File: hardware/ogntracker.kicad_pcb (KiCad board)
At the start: 2 copper layers, 82.7 x 56.6 mm, 54 parts, among them J1 ANT, J2 Micro USB, J3 IGC, U1 LM2936-3.3, Y1 12M

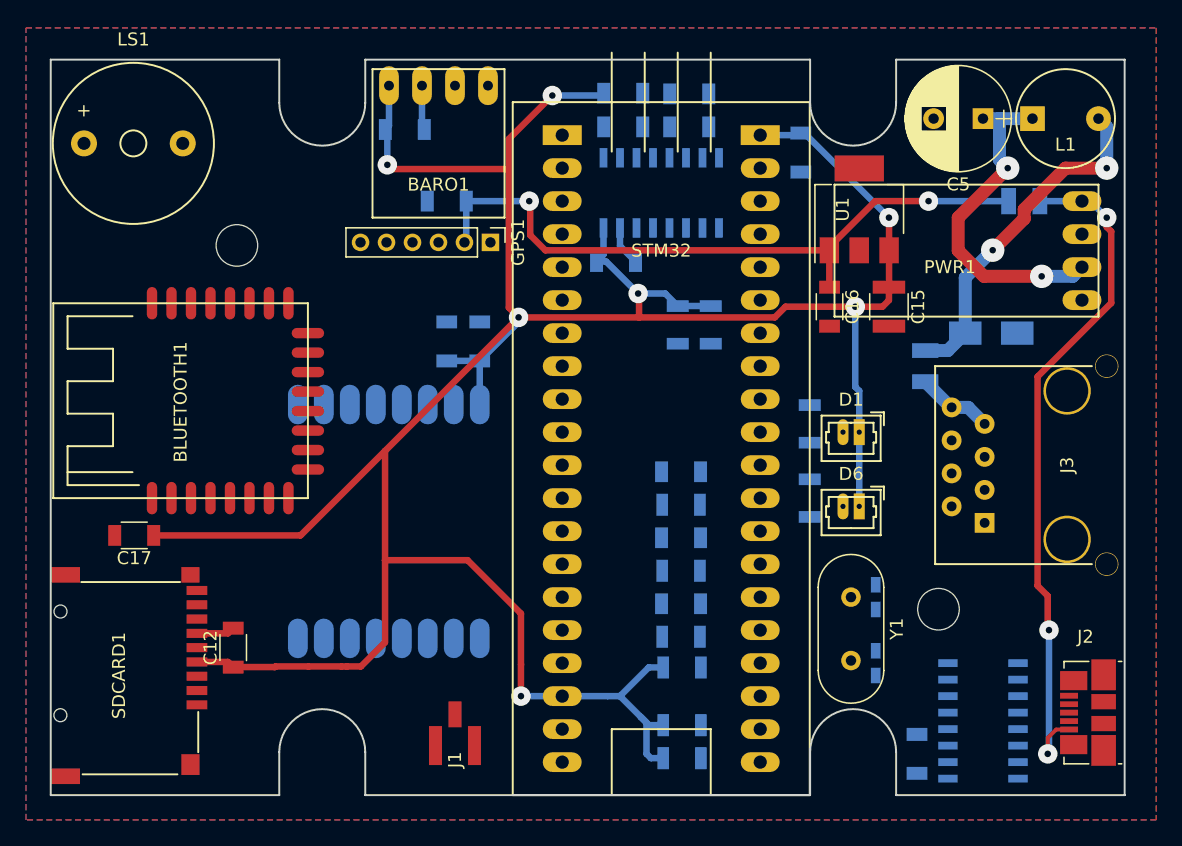
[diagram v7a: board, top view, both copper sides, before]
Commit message: Unverified attempt on standalone STM32 chip
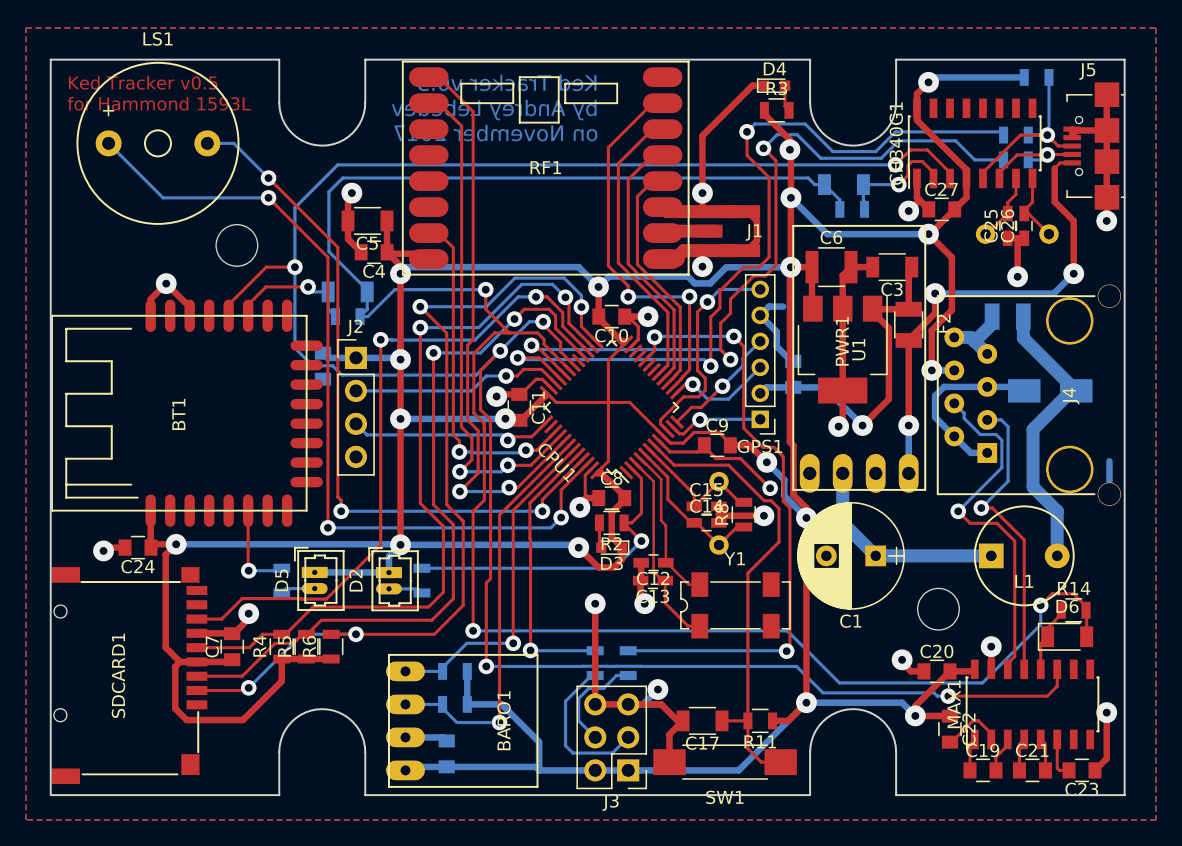
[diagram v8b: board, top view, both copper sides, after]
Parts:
- removed BLUETOOTH1: JDY-08, OGN Tracker:JDY-08
- removed MAX232: MAX3232, Housings_SOIC:SOIC-16_3.9x9.9mm_Pitch1.27mm
- removed RFM69HW1: RFM69HW, OGN Tracker:RFM69HW
- removed STM32: STM32DEVBOARD, OGN Tracker:STM32DEVBOARD_HandSoldering
- added BT1: JDY-08, OGN Tracker:JDY-08, F.Cu at (119.7, 78.1)
- added C19: 100nF, Capacitors_SMD:C_0805, F.Cu at (171.8, 98.1)
- added C20: 100nF, Capacitors_SMD:C_0805, F.Cu at (168.2, 90.5)
- added C21: 100nF, Capacitors_SMD:C_0805, F.Cu at (175.6, 98.1)
- added C22: 100nF, Capacitors_SMD:C_0805, F.Cu at (169.2, 94.9)
- added C23: 100nF, Capacitors_SMD:C_0805, F.Cu at (179.4, 98.1)
- added C24: 100nF, Capacitors_SMD:C_0805, F.Cu at (106.7, 81.0)
- added C25: 22pF, Capacitors_SMD:C_0603_HandSoldering, F.Cu at (173.7, 56.2)
- added C26: 22pF, Capacitors_SMD:C_0603_HandSoldering, F.Cu at (174.9, 56.2)
- added C27: 100nF, Capacitors_SMD:C_0805, F.Cu at (168.6, 54.9)
- added CPU1: STM32F103, Housings_QFP:LQFP-48_7x7mm_Pitch0.5mm, F.Cu at (143.2, 70.2)
- added D7: 1N4148, Diodes_SMD:D_1206, B.Cu at (122.9, 61.3)
- added D8: 1N4148, Diodes_SMD:D_1206, B.Cu at (161.1, 53.0)
- added J4: IGC, OGN Tracker:RJ45_SOCKET_SHLD, F.Cu at (178.4, 69.2)
- added J5: Micro USB, OGN Tracker:USB_Micro, F.Cu at (179.9, 50.0)
- added MAX1: MAX3232, Housings_SOIC:SOIC-16_3.9x9.9mm_Pitch1.27mm, F.Cu at (175.6, 93.0)
- added R11: 10K, Resistors_SMD:R_0805, F.Cu at (154.6, 94.3)
- added R12: 10K, Resistors_SMD:R_0805, B.Cu at (141.9, 89.8)
- added R13: 10K, Resistors_SMD:R_0805, B.Cu at (144.4, 89.8)
- added R14: 10K, Resistors_SMD:R_0805, F.Cu at (178.7, 85.8)
- added R15: 10K, Resistors_SMD:R_0805, B.Cu at (122.9, 63.2)
- added R16: 10K, Resistors_SMD:R_0805, B.Cu at (161.7, 54.9)
- added R17: 20, Resistors_SMD:R_0805, B.Cu at (174.3, 49.2)
- added R18: 20, Resistors_SMD:R_0805, B.Cu at (174.3, 51.1)
- added R19: 1.5K, Resistors_SMD:R_0805, B.Cu at (175.9, 44.8)
- added RF1: RFM69HW, OGN Tracker:RFM69HW, F.Cu at (138.1, 51.7)
- added SW1: RESET, Buttons_Switches_SMD:SW_SPST_REED_CT05-XXXX-G1, F.Cu at (151.9, 97.5)
- added Y2: 8MHz, Crystals:Crystal_HC49-4H_Vertical, B.Cu at (151.4, 80.8)
- added Y3: 12M, Crystals:Crystal_HC49-4H_Vertical, B.Cu at (176.8, 56.8)
- C1: value 100nF -> 330uF; footprint Capacitors_SMD:C_1206 -> Capacitors_ThroughHole:CP_Radial_D8.0mm_P3.80mm; moved to F.Cu
- C10, C11, C7, C8, C9: footprint Capacitors_SMD:C_1206 -> Capacitors_SMD:C_0805; moved to F.Cu
- C12: value 100nF -> 22pF; footprint Capacitors_SMD:C_1206 -> Capacitors_SMD:C_0603_HandSoldering
- C13, C14, CH340G1, F2: moved to F.Cu
- C15: value 47uF -> 22pF; footprint Capacitors_SMD:C_1210 -> Capacitors_SMD:C_0603_HandSoldering
- C16: value 1uF -> 100nF; footprint Capacitors_SMD:C_1206 -> Capacitors_SMD:C_0805; moved to B.Cu
- C17: value 100nF -> 1uF
- C18: footprint Capacitors_SMD:C_1206 -> Capacitors_SMD:C_0805
- C2: value 1uF -> 100nF; footprint Capacitors_SMD:C_1206 -> Capacitors_SMD:C_0805
- C3: value 100nF -> 1uF; moved to F.Cu
- C4: value 1uF -> 100nF; footprint Capacitors_SMD:C_1206 -> Capacitors_SMD:C_0805; moved to F.Cu
- C5: value 330uF -> 1uF; footprint Capacitors_ThroughHole:CP_Radial_D8.0mm_P3.80mm -> Capacitors_SMD:C_1206
- C6: value 100nF -> 47uF; footprint Capacitors_SMD:C_1206 -> Capacitors_SMD:C_1210; moved to F.Cu
- D1: value LED_STAT -> 1N4001; footprint OGN Tracker:Molex_PicoBlade_02x1.25mm_HandSoldering -> Diodes_SMD:D_SMA_Standard; moved to B.Cu
- D2: value 1N4001 -> STATUS_PANEL; footprint Diodes_SMD:D_SMA_Standard -> OGN Tracker:Molex_PicoBlade_02x1.25mm_HandSoldering; moved to F.Cu
- D3: value 1N4148 -> STATUS_SMD; footprint Diodes_SMD:D_1206 -> LEDs:LED_0603; moved to F.Cu
- D4: value 1N4148 -> PWR; footprint Diodes_SMD:D_1206 -> LEDs:LED_0603; moved to F.Cu
- D5: value 1N4148 -> LED_BT; footprint Diodes_SMD:D_1206 -> OGN Tracker:Molex_PicoBlade_02x1.25mm_HandSoldering; moved to F.Cu
- D6: value LED_BT -> 1N4148; footprint OGN Tracker:Molex_PicoBlade_02x1.25mm_HandSoldering -> Diodes_SMD:D_1206
- J2: value Micro USB -> SWD; footprint Connectors_Molex:USB_Micro-B_Molex_47346-0001 -> Pin_Headers:Pin_Header_Straight_1x04_Pitch2.54mm
- J3: value IGC -> BOOT; footprint OGN Tracker:RJ45_SOCKET_SHLD -> Pin_Headers:Pin_Header_Straight_2x03_Pitch2.54mm
- R1, R9: footprint Resistors_SMD:R_1206 -> Resistors_SMD:R_0805
- R10: value 82 -> 10K; footprint Resistors_SMD:R_1206 -> Resistors_SMD:R_0805
- R2, R3: value 10K -> 330; footprint Resistors_SMD:R_1206 -> Resistors_SMD:R_0805; moved to F.Cu
- R4, R5, R6: footprint Resistors_SMD:R_1206 -> Resistors_SMD:R_0805; moved to F.Cu
- R7: value 10K -> 82; footprint Resistors_SMD:R_1206 -> Resistors_SMD:R_0805
- R8: value 10K -> 1M; footprint Resistors_SMD:R_1206 -> Resistors_SMD:R_0805; moved to F.Cu
- Y1: value 12M -> 32.768K; footprint Crystals:Crystal_HC49-4H_Vertical -> Crystals:Crystal_SMD_SeikoEpson_MC306-4pin_8.0x3.2mm
- moved J2 62.5 mm to (123.5, 66.3), turned to 0 degrees
- moved C18 54.6 mm to (121.0, 67.0), turned to 270 degrees
- moved D2 49.9 mm to (126.0, 82.9), turned to 270 degrees
- moved C5 48.0 mm to (124.4, 55.8)
- moved BARO1 46.4 mm to (129.8, 94.3), turned to 270 degrees
- moved C17 46.0 mm to (150.2, 94.3)
- moved C16 45.3 mm to (130.5, 96.8), turned to 90 degrees
- moved J1 44.7 mm to (152.7, 56.6), turned to 180 degrees
- moved CH340G1 44.5 mm to (171.1, 49.8), turned to 90 degrees
- moved C1 42.8 mm to (163.5, 81.6)
- moved C7 41.8 mm to (114.0, 88.6), turned to 90 degrees
- moved J3 41.1 mm to (144.4, 98.1), turned to 180 degrees
- moved D4 35.5 mm to (155.7, 45.4)
- moved L1 33.8 mm to (174.9, 81.6)
- moved C4 33.7 mm to (124.9, 58.2), turned to 180 degrees
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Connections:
- C1 pad 1: /5V_PROT -> /SUP_CLEAN
- C10 pad 2: Net-(C10-Pad2) -> 3.3V
- C11 pad 1: 3.3V -> Earth
- C11 pad 2: Earth -> 3.3V
- C12 pad 1: 3.3V -> /RTCOUT
- C13 pad 1: Earth -> /RTCIN
- C13 pad 2: /Console/USB_XI -> Earth
- C14 pad 1: Earth -> /OSCIN
- C14 pad 2: /Console/USB_XO -> Earth
- C15 pad 1: 3.3V -> /OSCOUT
- C16 pad 1: /5V_PROT -> 3.3V
- C17 pad 1: 3.3V -> /RESET
- C18 pad 1: Earth -> 3.3V
- C18 pad 2: 3.3V -> Earth
- C2 pad 1: 3.3V -> /5V_PROT
- C3 pad 1: 3.3V -> /5V_PROT
- C4 pad 1: Earth -> 3.3V
- C4 pad 2: 3.3V -> Earth
- C5 pad 1: /SUP_CLEAN -> 3.3V
- C6 pad 1: Net-(C6-Pad1) -> 3.3V
- C6 pad 2: Net-(C6-Pad2) -> Earth
- C7 pad 1: Earth -> 3.3V
- C7 pad 2: 3.3V -> Earth
- C8 pad 1: Net-(C8-Pad1) -> Earth
- C8 pad 2: Net-(C8-Pad2) -> 3.3V
- C9 pad 1: 3.3V -> Earth
- C9 pad 2: Net-(C9-Pad2) -> 3.3V
- CH340G1 pad 5: /Console/USB_D+ -> /Console/CON_USB_D+
- CH340G1 pad 6: /Console/USB_D- -> /Console/CON_USB_D-
- D1 pad 1: 3.3V -> /SUP_PROT
- D1 pad 2: Net-(D1-Pad2) -> Earth
- D2 pad 1: /SUP_PROT -> 3.3V
- D2 pad 2: Earth -> Net-(D2-Pad2)
- D3 pad 1: /Console/MAX232_TX -> 3.3V
- D3 pad 2: /CON1_RXD -> Net-(D3-Pad2)
- D4 pad 1: /Console/BT_TX -> Earth
- D4 pad 2: /CON1_RXD -> Net-(D4-Pad2)
- D5 pad 1: /Console/USB_TX -> 3.3V
- D5 pad 2: /CON1_RXD -> Net-(D5-Pad2)
- D6 pad 1: 3.3V -> /Console/MAX232_TX
- D6 pad 2: Net-(D6-Pad2) -> /CON1_RXD
- J2 pad 1: 5V -> 3.3V
- J2 pad 2: /Console/USB_D- -> /SWDIO
- J2 pad 3: /Console/USB_D+ -> /SWDCLK
- J2 pad 4: (no net) -> Earth
- J3 pad 1: Earth -> 3.3V
- J3 pad 2: Earth -> 3.3V
- J3 pad 3: /Console/RS232_RX -> Net-(J3-Pad3)
- J3 pad 4: /Console/RS232_TX -> Net-(J3-Pad4)
- J3 pad 6: 3.3V -> Earth
- R1 pad 1: /LED -> /STAT_LED
- R1 pad 2: Net-(D1-Pad2) -> Net-(D2-Pad2)
- R10 pad 1: /Console/BT_STATUS -> /BARO_SCL
- R10 pad 2: Net-(D6-Pad2) -> 3.3V
- R2 pad 1: /BARO_SDA -> /STAT_LED
- R2 pad 2: 3.3V -> Net-(D3-Pad2)
- R3 pad 1: /BARO_SCL -> 3.3V
- R3 pad 2: 3.3V -> Net-(D4-Pad2)
- R4 pad 1: /Console/MAX232_TX -> 3.3V
- R4 pad 2: /CON1_RXD -> /SD_SCK
- R5 pad 1: /Console/BT_TX -> 3.3V
- R5 pad 2: /CON1_RXD -> /SD_MOSI
- R6 pad 1: /CON1_RXD -> 3.3V
- R6 pad 2: /Console/USB_TX -> /SD_CS
- R7 pad 1: 3.3V -> /Console/BT_STATUS
- R7 pad 2: /SD_SCK -> Net-(D5-Pad2)
- R8 pad 1: 3.3V -> /OSCIN
- R8 pad 2: /SD_MOSI -> /OSCOUT
- R9 pad 1: 3.3V -> /BARO_SDA
- R9 pad 2: /SD_CS -> 3.3V
- Y1 pad 1: /Console/USB_XO -> /RTCIN
- Y1 pad 2: /Console/USB_XI -> (no net)
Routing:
- net Earth: track 9.49 -> 179.8 mm, vias 0 -> 21
- net /CON1_TXD: track 0.00 -> 169.3 mm, vias 0 -> 6
- net /CON1_RXD: track 0.00 -> 153.7 mm, vias 0 -> 3
- net 3.3V: track 232.5 -> 377.6 mm, vias 7 -> 18
- net /SD_CS: track 0.00 -> 67.7 mm, vias 0 -> 4
- net /BUZ_IN: track 0.00 -> 64.6 mm, vias 0 -> 3
- net /USB_D+: track 0.00 -> 62.1 mm, vias 0 -> 3
- net /SD_SCK: track 0.00 -> 59.5 mm, vias 0 -> 2
- net /USB_D-: track 0.00 -> 59.3 mm, vias 0 -> 3
- net /SD_MOSI: track 0.00 -> 56.7 mm, vias 0 -> 2
- net /BUZ_OUT: track 0.00 -> 54.8 mm, vias 0 -> 3
- net /SD_MISO: track 0.00 -> 52.0 mm, vias 0 -> 2
- net /BOOT1: track 0.00 -> 47.1 mm, vias 0 -> 3
- net /CHIP_RESET: track 0.00 -> 44.5 mm, vias 0 -> 2
- net /INT_REQ: track 0.00 -> 39.5 mm, vias 0 -> 2
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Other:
- net class ANT: trace_width 3.23 -> 1; via_dia 1.5 -> 1.2; via_drill 0.5 -> 0.6
- net class Default: clearance 0.2 -> 0.24; trace_width 0.3 -> 0.24; via_dia 1.5 -> 1.2; via_drill 0.5 -> 0.6
- net class HV: via_drill 0.5 -> 0.6
- net class PWR: clearance 0.2 -> 0.24; via_dia 1.5 -> 1.6; via_drill 0.5 -> 0.6
- rule trace_clearance: 0.2 -> 0.24
- rule trace_min: 0 -> 0.2
- board text added: "Ked Tracker v0.5 by Andrey Lebedev on November 2017"
- board text added: "Ked Tracker v0.5 for Hammond 1593L"
